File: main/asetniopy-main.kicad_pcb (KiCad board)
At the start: 2 copper layers, 32 x 33 mm, 20 parts, among them J1 Conn_01x02, J2 Conn_01x02, J3 Conn_01x02, J4 Conn_01x02, J5 Conn_01x02, J6 Power/Reset, J7 BAT+, J8 BAT-, U1 ProMicro, U2 LSM6DSO

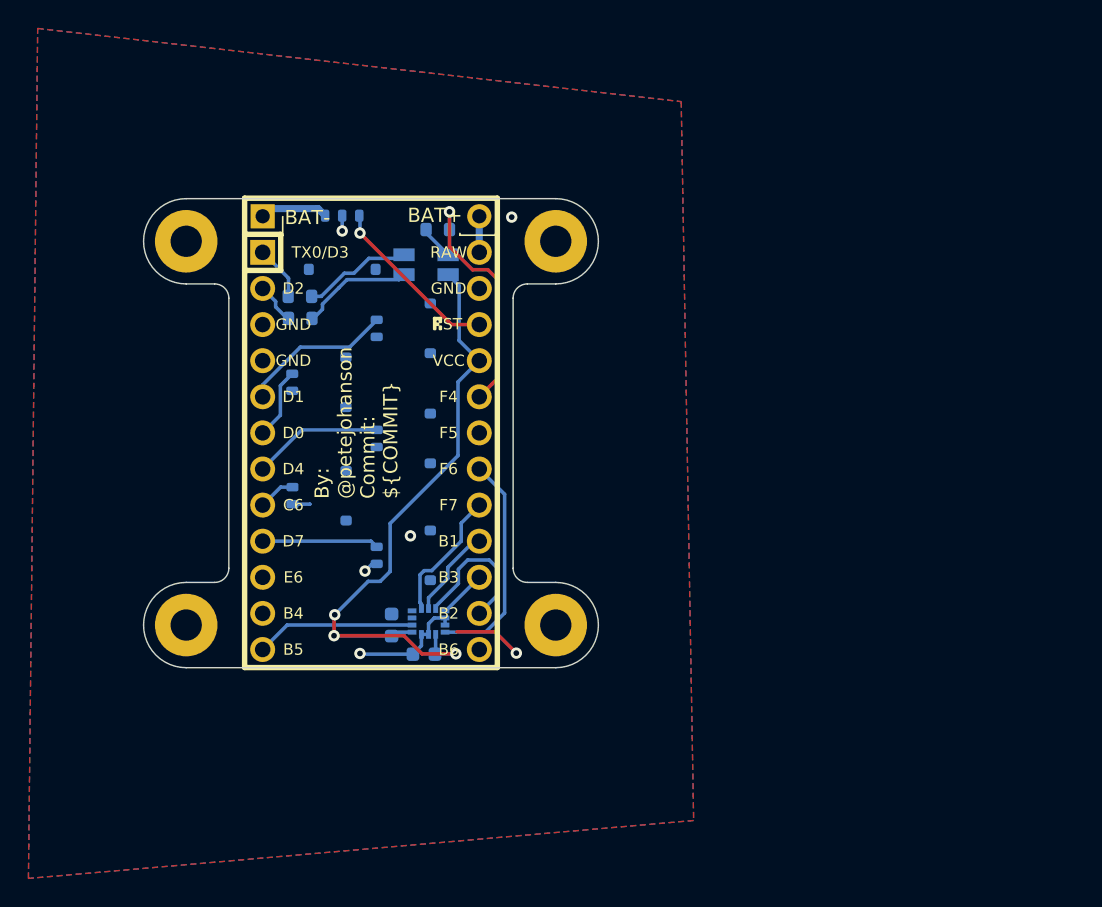
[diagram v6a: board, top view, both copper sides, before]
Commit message: Left and right boards, joined via mouse bites.
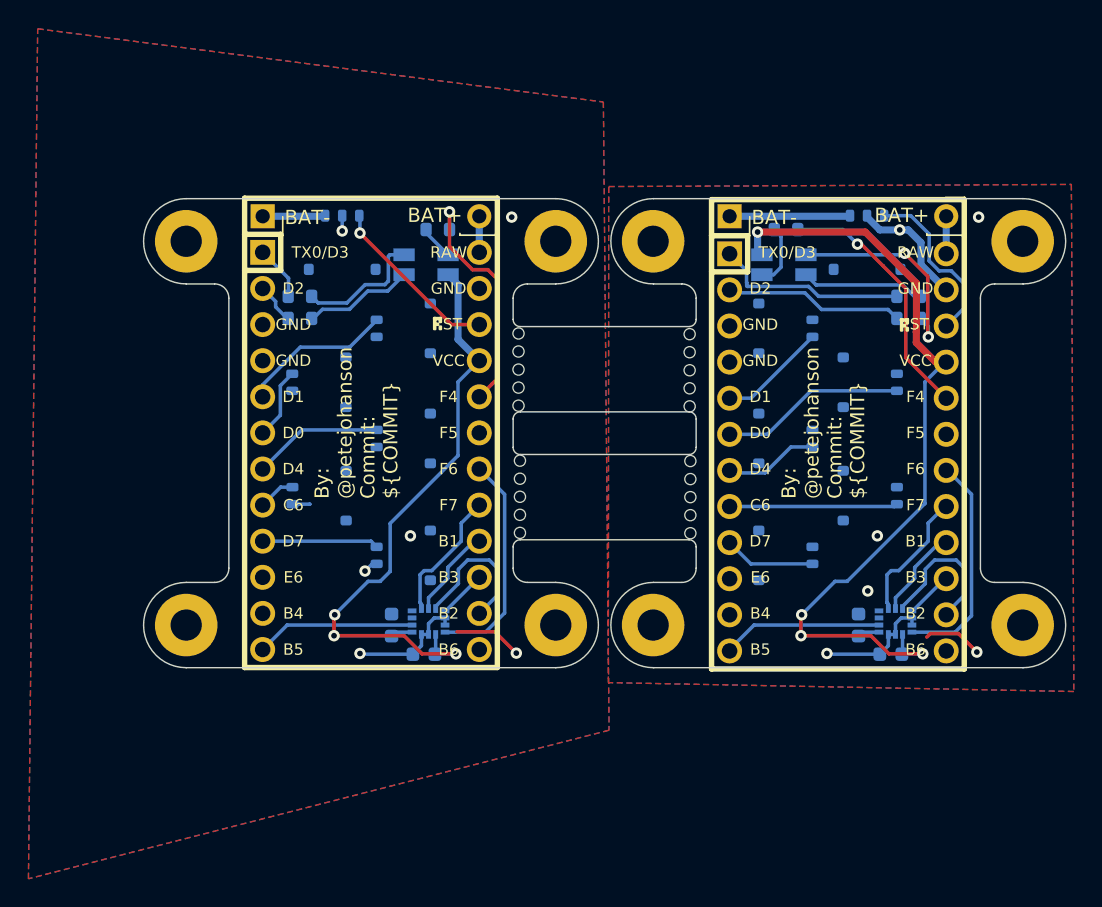
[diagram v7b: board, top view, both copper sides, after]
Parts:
- added C2: 100nF, Capacitor_SMD:C_0603_1608Metric, B.Cu at (136.6, 115.5)
- added C4: 100nF, Capacitor_SMD:C_0603_1608Metric, B.Cu at (134.3, 113.5)
- added D2: LED_ABGR, LED_SMD:LED_RGB_Wuerth-PLCC4_3.2x2.8mm_150141M173100, B.Cu at (129.1, 88.2)
- added H5: MountingHole, MountingHole:MountingHole_2.2mm_M2_Pad, F.Cu at (119.8, 86.5)
- added H6: MountingHole, MountingHole:MountingHole_2.2mm_M2_Pad, F.Cu at (145.8, 86.5)
- added H7: MountingHole, MountingHole:MountingHole_2.2mm_M2_Pad, F.Cu at (119.8, 113.5)
- added H8: MountingHole, MountingHole:MountingHole_2.2mm_M2_Pad, F.Cu at (145.8, 113.5)
- added J10: Conn_01x02, Connector_Molex:Molex_Pico-EZmate_78171-0002_1x02-1MP_P1.20mm_Vertical, B.Cu at (135.1, 96.4)
- added J11: Conn_01x02, Connector_Molex:Molex_Pico-EZmate_78171-0002_1x02-1MP_P1.20mm_Vertical, B.Cu at (129.2, 100.4)
- added J12: Conn_01x02, Connector_Molex:Molex_Pico-EZmate_78171-0002_1x02-1MP_P1.20mm_Vertical, B.Cu at (135.1, 104.4)
- added J13: Conn_01x02, Connector_Molex:Molex_Pico-EZmate_78171-0002_1x02-1MP_P1.20mm_Vertical, B.Cu at (129.2, 108.6)
- added J14: BAT+, Connector_PinSocket_2.54mm:PinSocket_1x01_P2.54mm_Vertical, F.Cu at (140.4, 84.7)
- added J15: BAT-, Connector_PinSocket_2.54mm:PinSocket_1x01_P2.54mm_Vertical, F.Cu at (125.3, 84.8)
- added J16: Power/Reset, Connector_Molex:Molex_Pico-EZmate_78171-0003_1x03-1MP_P1.20mm_Vertical, B.Cu at (134.9, 86.6)
- added J9: Conn_01x02, Connector_Molex:Molex_Pico-EZmate_78171-0002_1x02-1MP_P1.20mm_Vertical, B.Cu at (129.2, 92.6)
- added R4: 68, Resistor_SMD:R_0603_1608Metric, B.Cu at (137.8, 90.4)
- added R5: 22, Resistor_SMD:R_0603_1608Metric, B.Cu at (137.8, 91.9)
- added R6: 22, Resistor_SMD:R_0603_1608Metric, B.Cu at (129.2, 85.7)
- added REF**: breakaway-mousebites, Keebio-Parts:breakaway-mousebites, F.Cu at (122.7, 104.5)
- added REF**: breakaway-mousebites, Keebio-Parts:breakaway-mousebites, F.Cu at (122.7, 95.6)
- added REF**: breakaway-mousebites, Keebio-Parts:breakaway-mousebites, F.Cu at (110.2, 104.5)
- added REF**: breakaway-mousebites, Keebio-Parts:breakaway-mousebites, F.Cu at (110.1, 95.5)
- added U3: ProMicro, Keebio-Parts:ArduinoProMicro, F.Cu at (132.8, 101.3)
- added U4: LSM6DSO, main:PQFN50P250X300X86-14N, B.Cu at (136.9, 113.2)
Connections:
- net Net-(J7-Pad1) renamed BAT+
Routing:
- net VCCQ: track 0.00 -> 63.0 mm, vias 0 -> 4
- net GND1: track 0.00 -> 21.5 mm, vias 0 -> 6
- net LED_B_r: track 0.00 -> 18.2 mm, vias 0 -> 1
- net ACC_INT1_r: track 0.00 -> 15.7 mm
- net Net-(D2-Pad3): track 0.00 -> 15.1 mm, vias 0 -> 2
- net LED_R_r: track 0.00 -> 13.6 mm
- net SW2_r: track 0.00 -> 13.0 mm
- net LED_G_r: track 0.00 -> 12.6 mm
- net RESET_r: track 0.00 -> 12.2 mm
- net SW4_r: track 0.00 -> 11.8 mm
- net ACC_INT2_r: track 0.00 -> 11.2 mm
- net COPI_r: track 0.00 -> 10.4 mm
- net ACC_CS_r: track 0.00 -> 9.36 mm
- net Net-(D2-Pad4): track 0.00 -> 8.68 mm
- net BAT-_r: track 0.00 -> 8.49 mm
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- added copper zone on B.Cu, net GND1
- added copper zone on F.Cu, net GND1
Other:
- board size 32 x 33 mm -> 64.9 x 33 mm
